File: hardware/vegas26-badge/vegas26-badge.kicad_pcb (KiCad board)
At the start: 2 copper layers, 100 x 145 mm, 41 parts, among them J1 FH34SRJ-24S-0.5SH(50)/(99) / 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, J2 AUDIO, J3 TC2050-IDC-NL / DNL, Q1 BSS138

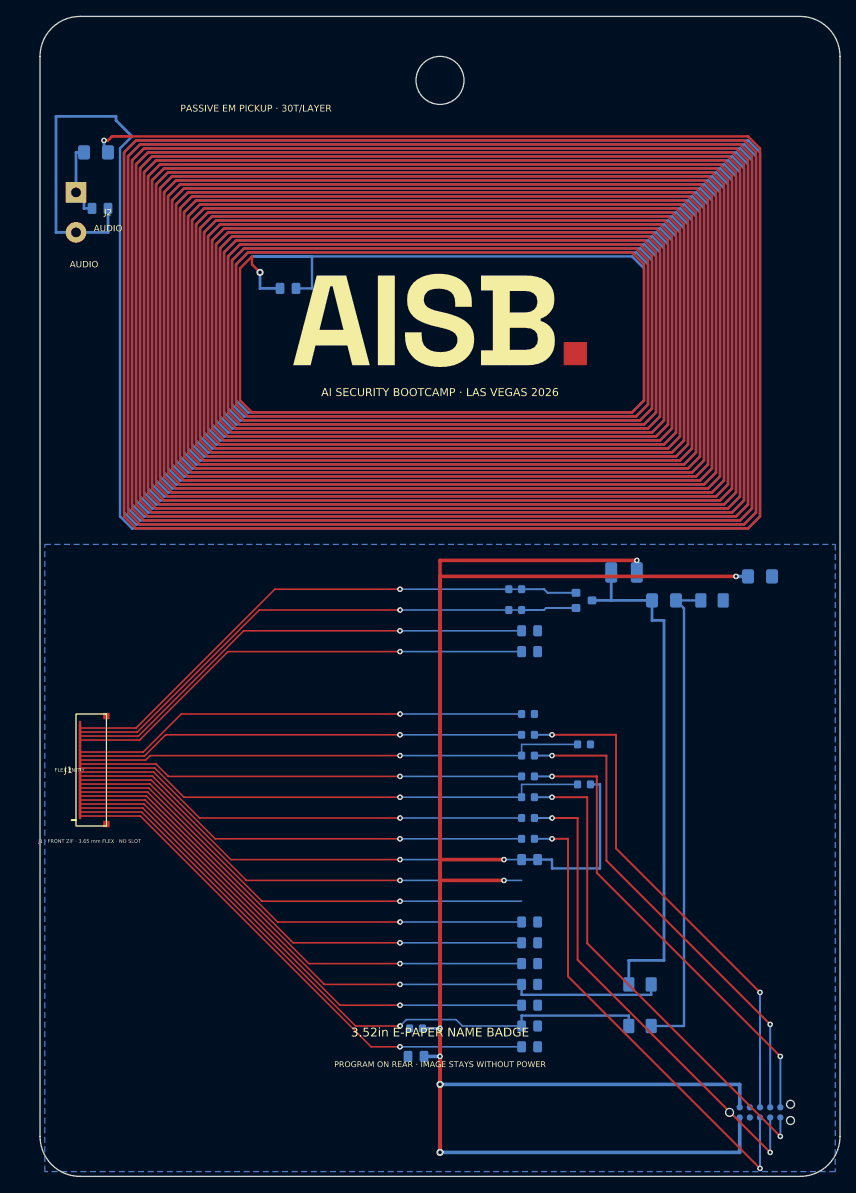
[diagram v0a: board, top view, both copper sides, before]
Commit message: Simplify ESP32 add-on to passive ribbon mount
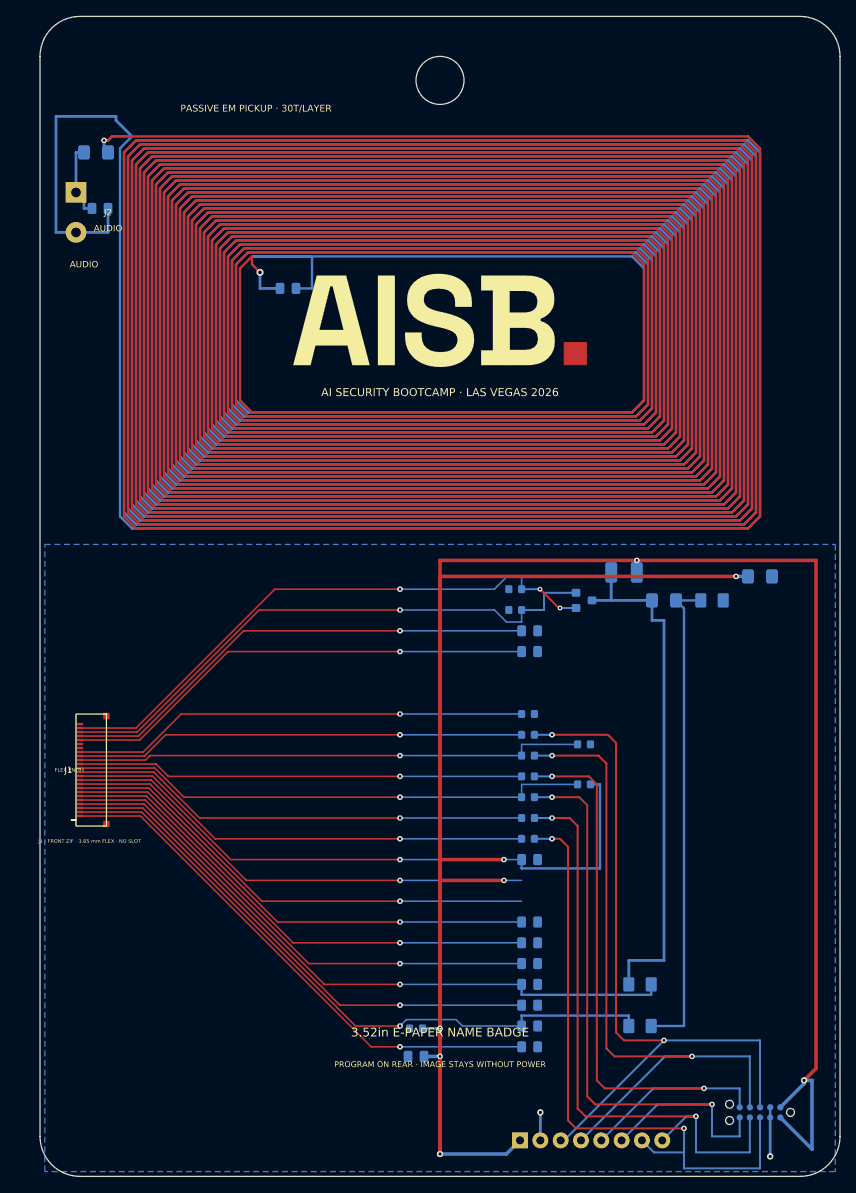
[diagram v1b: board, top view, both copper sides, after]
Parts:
- removed the MOD1 at (20.2, 120.9)
- removed the R3 at (59.4, 74.2)
- removed the R5 at (61.0, 102.8)
- removed the R6 at (61.0, 100.2)
- removed the R7 at (61.0, 97.6)
- added C13: 100nF, Badge:0603_C13, B.Cu at (47.0, 126.5)
- added C14: 1uF 10V, Badge:0805_C14, B.Cu at (61.2, 105.4)
- added C15: 1uF 25V / DNP, Badge:0805_C15, B.Cu at (61.2, 76.8)
- added D1: MBR0530, Badge:D_SOD-123, B.Cu at (84.0, 73.0)
- added J4: 1x08 P2.54 / OPTIONAL / DNP, Badge:ESP_Ribbon_1x08_P2.54mm, B.Cu at (60.0, 140.5)
- added L2: 68uH, Badge:1210_L2, B.Cu at (73.0, 69.5)
- added MH1: 4x 2.2x6 NPTH CRADLE SLOTS, Badge:ESP32_Cradle_Strap_Slots, B.Cu at (0.00, 0.00)
- C10: renamed from C15; value 1uF 25V / DNP -> 1uF 25V; footprint Badge:0805_C15 -> Badge:0805_C10
- C11: renamed from L2; value 68uH -> 1uF 25V; footprint Badge:1210_L2 -> Badge:0805_C11
- C12: renamed from D1; value MBR0530 -> 10uF 10V; footprint Badge:D_SOD-123 -> Badge:0805_C12
- C2: renamed from C7; value 1uF 25V -> 4.7uF 50V; footprint Badge:0805_C7 -> Badge:1206_C2
- C3: renamed from C8; value 1uF 25V -> 4.7uF 50V; footprint Badge:0805_C8 -> Badge:1206_C3
- C4: renamed from C9; footprint Badge:0805_C9 -> Badge:0805_C4
- C5: renamed from C10; value 1uF 25V -> 1uF 10V; footprint Badge:0805_C10 -> Badge:0805_C5
- C6: renamed from C11; footprint Badge:0805_C11 -> Badge:0805_C6
- C7: renamed from C12; value 10uF 10V -> 1uF 25V; footprint Badge:0805_C12 -> Badge:0805_C7
- C8: renamed from C13; value 100nF -> 1uF 25V; footprint Badge:0603_C13 -> Badge:0805_C8
- C9: renamed from C14; value 1uF 10V -> 1uF 25V; footprint Badge:0805_C14 -> Badge:0805_C9
- MOD1: renamed from R4; value 10k -> WAVESHARE E-PAPER ESP32 DRIVER BOARD V3 / OPTIONAL; footprint Badge:0603_R4 -> Badge:Waveshare_ESP32_Driver_Board_V3_Header_Clear_Cradle_Bay
- R10: renamed from C3; value 4.7uF 50V -> 1k; footprint Badge:1206_C3 -> Badge:0603_R10
- R11: renamed from C4; value 1uF 25V -> 100k; footprint Badge:0805_C4 -> Badge:0603_R11
- R12: renamed from C5; value 1uF 10V -> 100k; footprint Badge:0805_C5 -> Badge:0603_R12
- R13: renamed from C6; value 1uF 25V -> 0R; footprint Badge:0805_C6 -> Badge:0603_R13
- R3: renamed from R8; value 100R -> 3R; footprint Badge:0603_R8 -> Badge:0603_R3
- R4: renamed from R9; value 100R -> 10k; footprint Badge:0603_R9 -> Badge:0603_R4
- R5: renamed from R10; value 1k -> 100R; footprint Badge:0603_R10 -> Badge:0603_R5
- R6: renamed from R11; value 100k -> 100R; footprint Badge:0603_R11 -> Badge:0603_R6
- R7: renamed from R12; value 100k -> 100R; footprint Badge:0603_R12 -> Badge:0603_R7
- R8: renamed from R13; value 0R -> 100R; footprint Badge:0603_R13 -> Badge:0603_R8
- R9: renamed from C2; value 4.7uF 50V -> 100R; footprint Badge:1206_C2 -> Badge:0603_R9
- moved C12 68.0 mm to (47.0, 130.0)
- moved MOD1 62.9 mm to (20.2, 120.9)
- moved C11 60.5 mm to (61.2, 128.8)
- moved C2 56.3 mm to (90.0, 70.0)
- moved C3 50.9 mm to (78.0, 73.0)
- moved C10 49.4 mm to (61.2, 126.2)
- moved C4 44.2 mm to (61.2, 79.4)
- moved R9 36.6 mm to (61.0, 92.4)
- moved R13 28.6 mm to (61.0, 87.2)
- moved R10 23.9 mm to (61.0, 89.8)
- moved R12 23.2 mm to (68.0, 91.0)
- moved R4 20.9 mm to (59.4, 71.6)
- moved R3 20.9 mm to (59.4, 74.2)
- moved C7 18.3 mm to (61.2, 118.4)
- moved C9 18.2 mm to (61.2, 123.6)
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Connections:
- C10 pad 1: LEGACY_NC -> VGL
- C11 pad 1: SW -> VCOM
- C11 pad 2: 3V3 -> DGND
- C12 pad 2: CFLY -> 3V3
- C2 pad 1: VSH -> 3V3
- C3 pad 1: VGH -> SW
- C3 pad 2: DGND -> CFLY
- C4 pad 1: VSL -> VDHR
- C5 pad 1: VGL -> VDDD
- C6 pad 1: VCOM -> VPP
- C7 pad 1: DGND -> VSH
- C7 pad 2: 3V3 -> DGND
- C8 pad 1: DGND -> VGH
- C8 pad 2: 3V3 -> DGND
- C9 pad 1: 3V3 -> VSL
- R10 pad 1: SW -> EPD_BUSY
- R10 pad 2: CFLY -> EXT_BUSY
- R11 pad 1: VDHR -> EPD_CS
- R11 pad 2: DGND -> 3V3
- R12 pad 1: VDDD -> EPD_RST
- R13 pad 1: VPP -> BS
- R3 pad 1: EPD_DC -> DGND
- R3 pad 2: EXT_DC -> RESE
- R4 pad 1: EPD_RST -> DGND
- R4 pad 2: EXT_RST -> GDR
- R5 pad 1: EPD_BUSY -> EPD_MOSI
- R5 pad 2: EXT_BUSY -> EXT_MOSI
- R6 pad 1: EPD_CS -> EPD_CLK
- R6 pad 2: 3V3 -> EXT_CLK
- R7 pad 1: EPD_RST -> EPD_CS
- R7 pad 2: DGND -> EXT_CS
- R8 pad 1: BS -> EPD_DC
- R8 pad 2: DGND -> EXT_DC
- R9 pad 1: 3V3 -> EPD_RST
- R9 pad 2: DGND -> EXT_RST
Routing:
- net 3V3: track 382.9 -> 419.4 mm
- net EXT_BUSY: track 64.2 -> 91.7 mm
- net EXT_RST: track 61.4 -> 88.0 mm
- net EXT_DC: track 58.7 -> 81.4 mm
- net EXT_MOSI: track 61.7 -> 83.5 mm
- net EXT_CS: track 61.4 -> 82.4 mm
- net EXT_CLK: track 61.5 -> 77.4 mm
- net DGND: track 61.1 -> 70.7 mm, vias 1 -> 3
- net RESE: track 68.4 -> 72.6 mm
- net GDR: track 69.4 -> 72.3 mm, vias 1 -> 3
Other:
- board text added: "ONE CONTROLLER · 3V3 ONLY"
- board text added: "REV 2 · VERIFY PANEL/J1 + ESP CRADLE"
- board text removed: "ONE 3V3 SOURCE ONLY"
- board text removed: "REV 1 · PANEL/J1 FIT MUST BE VERIFIED"

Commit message: Save KiCad 10 badge board state
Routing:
- net 3V3: track 419.4 -> 407.2 mm
- net DGND: track 70.7 -> 80.1 mm, vias 3 -> 4

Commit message: Enlarge badge logo and add rear QR
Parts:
- moved ? 4.35 mm to (71.1, 43.2)
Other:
- board text added: "aisb.dev/badge0"
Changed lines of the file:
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@@
 		(at 50 38)
 		(property "Reference" "LOGO1"
-			(at 0 -7.2 0)
+			(at 0 -9 0)
 			(layer "F.Fab")
 			(effects
@@
 		)
 		(property "Value" "AISB OFFICIAL WORDMARK"
-			(at 0 7.2 0)
+			(at 0 9 0)
 			(layer "F.Fab")
 			(effects
@@
 		(fp_poly
 			(pts
-				(xy -7.764 5.6) (xy -7.764 -5.6) (xy -5.652 -5.6) (xy -5.652 5.6) (xy -7.764 5.6)
+				(xy -9.705 7) (xy -9.705 -7) (xy -7.065 -7) (xy -7.065 7) (xy -9.705 7)
 			)
 			(stroke
@@
 		(fp_poly
 			(pts
-				(xy -18.356 5.6) (xy -15.412 -5.6) (xy -11.732 -5.6) (xy -8.788 5.6) (xy -10.964 5.6) (xy -11.572 3.136)
-				(xy -15.076 3.136) (xy -15.076 1.184) (xy -12.068 1.184) (xy -13.428 -4.272) (xy -13.716 -4.272)
-				(xy -15.076 1.184) (xy -15.076 3.136) (xy -15.572 3.136) (xy -16.18 5.6) (xy -18.356 5.6)
+				(xy -22.945 7) (xy -19.265 -7) (xy -14.665 -7) (xy -10.985 7) (xy -13.705 7) (xy -14.465 3.92)
+				(xy -18.845 3.92) (xy -18.845 1.48) (xy -15.085 1.48) (xy -16.785 -5.34) (xy -17.145 -5.34)
+				(xy -18.845 1.48) (xy -18.845 3.92) (xy -19.465 3.92) (xy -20.225 7) (xy -22.945 7)
 			)
 			(stroke
@@
 		(fp_poly
 			(pts
-				(xy 5.132 5.6) (xy 5.132 3.744) (xy 6.604 3.744) (xy 6.604 -3.744) (xy 5.132 -3.744) (xy 5.132 -5.6)
-				(xy 10.892 -5.6) (xy 11.545 -5.562) (xy 12.14 -5.447) (xy 12.676 -5.256) (xy 13.145 -4.995) (xy 13.54 -4.669)
-				(xy 13.86 -4.28) (xy 14.096 -3.831) (xy 14.237 -3.327) (xy 14.284 -2.768) (xy 14.284 -2.608) (xy 14.252 -2.127)
-				(xy 14.156 -1.708) (xy 13.996 -1.352) (xy 13.682 -0.92) (xy 13.316 -0.6) (xy 12.934 -0.374) (xy 12.572 -0.224)
-				(xy 12.572 0.064) (xy 12.94 0.202) (xy 13.34 0.424) (xy 13.726 0.746) (xy 14.052 1.184) (xy 14.216 1.548)
-				(xy 14.315 1.98) (xy 14.348 2.48) (xy 14.348 2.64) (xy 14.3 3.229) (xy 14.156 3.76) (xy 13.916 4.232)
-				(xy 13.592 4.64) (xy 13.194 4.979) (xy 12.724 5.248) (xy 12.19 5.444) (xy 11.6 5.561) (xy 10.956 5.6)
-				(xy 8.716 5.6) (xy 8.716 -0.992) (xy 10.668 -0.992) (xy 11.266 -1.076) (xy 11.748 -1.328) (xy 12.066 -1.728)
-				(xy 12.172 -2.256) (xy 12.172 -2.416) (xy 12.068 -2.954) (xy 11.756 -3.352) (xy 11.276 -3.598) (xy 10.668 -3.68)
-				(xy 8.716 -3.68) (xy 8.716 -0.992) (xy 8.716 5.6) (xy 8.716 3.68) (xy 10.7 3.68) (xy 11.322 3.596)
-				(xy 11.812 3.344) (xy 12.13 2.936) (xy 12.236 2.384) (xy 12.236 2.224) (xy 12.132 1.672) (xy 11.82 1.264)
-				(xy 11.332 1.012) (xy 10.7 0.928) (xy 8.716 0.928) (xy 8.716 3.68) (xy 8.716 5.6) (xy 5.132 5.6)
+				(xy 6.415 7) (xy 6.415 4.68) (xy 8.255 4.68) (xy 8.255 -4.68) (xy 6.415 -4.68) (xy 6.415 -7)
+				(xy 13.615 -7) (xy 14.4313 -6.9525) (xy 15.175 -6.8087) (xy 15.845 -6.57) (xy 16.4312 -6.2438) (xy 16.925 -5.8362)
+				(xy 17.325 -5.35) (xy 17.62 -4.7888) (xy 17.7963 -4.1587) (xy 17.855 -3.46) (xy 17.855 -3.26) (xy 17.815 -2.6587)
+				(xy 17.695 -2.135) (xy 17.495 -1.69) (xy 17.1025 -1.15) (xy 16.645 -0.75) (xy 16.1675 -0.4675) (xy 15.715 -0.28)
+				(xy 15.715 0.08) (xy 16.175 0.2525) (xy 16.675 0.53) (xy 17.1575 0.9325) (xy 17.565 1.48) (xy 17.77 1.935)
+				(xy 17.8938 2.475) (xy 17.935 3.1) (xy 17.935 3.3) (xy 17.875 4.0362) (xy 17.695 4.7) (xy 17.395 5.29)
+				(xy 16.99 5.8) (xy 16.4925 6.2237) (xy 15.905 6.56) (xy 15.2375 6.805) (xy 14.5 6.9512) (xy 13.695 7)
+				(xy 10.895 7) (xy 10.895 -1.24) (xy 13.335 -1.24) (xy 14.0825 -1.345) (xy 14.685 -1.66) (xy 15.0825 -2.16)
+				(xy 15.215 -2.82) (xy 15.215 -3.02) (xy 15.085 -3.6925) (xy 14.695 -4.19) (xy 14.095 -4.4975) (xy 13.335 -4.6)
+				(xy 10.895 -4.6) (xy 10.895 -1.24) (xy 10.895 7) (xy 10.895 4.6) (xy 13.375 4.6) (xy 14.1525 4.495)
+				(xy 14.765 4.18) (xy 15.1625 3.67) (xy 15.295 2.98) (xy 15.295 2.78) (xy 15.165 2.09) (xy 14.775 1.58)
+				(xy 14.165 1.265) (xy 13.375 1.16) (xy 10.895 1.16) (xy 10.895 4.6) (xy 10.895 7) (xy 6.415 7)
 			)
 			(stroke
@@
 		(fp_poly
 			(pts
-				(xy 0.028 5.824) (xy -0.601 5.795) (xy -1.192 5.708) (xy -1.745 5.563) (xy -2.26 5.36) (xy -2.729 5.103)
-				(xy -3.144 4.796) (xy -3.505 4.439) (xy -3.812 4.032) (xy -4.057 3.578) (xy -4.232 3.08) (xy -4.337 2.538)
-				(xy -4.372 1.952) (xy -4.372 1.504) (xy -2.292 1.504) (xy -2.292 1.952) (xy -2.223 2.568) (xy -2.015 3.072)
-				(xy -1.668 3.464) (xy -1.202 3.744) (xy -0.637 3.912) (xy 0.028 3.968) (xy 0.692 3.92) (xy 1.233 3.776)
-				(xy 1.652 3.536) (xy 1.95 3.221) (xy 2.128 2.853) (xy 2.188 2.432) (xy 2.122 2.012) (xy 1.924 1.68)
-				(xy 1.6 1.418) (xy 1.156 1.208) (xy 0.796 1.088) (xy 0.388 0.973) (xy -0.068 0.864) (xy -0.436 0.784)
-				(xy -0.991 0.648) (xy -1.506 0.494) (xy -1.979 0.323) (xy -2.412 0.136) (xy -2.919 -0.153) (xy -3.34 -0.497)
-				(xy -3.676 -0.896) (xy -3.92 -1.365) (xy -4.067 -1.92) (xy -4.116 -2.56) (xy -4.062 -3.21) (xy -3.899 -3.794)
-				(xy -3.628 -4.312) (xy -3.258 -4.76) (xy -2.8 -5.133) (xy -2.252 -5.432) (xy -1.789 -5.604) (xy -1.286 -5.726)
-				(xy -0.744 -5.8) (xy -0.164 -5.824) (xy 0.42 -5.799) (xy 0.97 -5.722) (xy 1.488 -5.595) (xy 1.972 -5.416)
-				(xy 2.415 -5.187) (xy 2.808 -4.908) (xy 3.151 -4.579) (xy 3.444 -4.2) (xy 3.679 -3.771) (xy 3.846 -3.29)
-				(xy 3.947 -2.758) (xy 3.98 -2.176) (xy 3.98 -1.696) (xy 1.9 -1.696) (xy 1.9 -2.176) (xy 1.838 -2.754)
-				(xy 1.652 -3.208) (xy 1.35 -3.548) (xy 0.94 -3.784) (xy 0.432 -3.922) (xy -0.164 -3.968) (xy -0.748 -3.928)
-				(xy -1.22 -3.808) (xy -1.58 -3.608) (xy -1.922 -3.182) (xy -2.036 -2.624) (xy -1.982 -2.24) (xy -1.82 -1.92)
-				(xy -1.55 -1.656) (xy -1.172 -1.44) (xy -0.68 -1.26) (xy -0.068 -1.104) (xy 0.3 -1.024) (xy 0.881 -0.887)
-				(xy 1.422 -0.732) (xy 1.924 -0.559) (xy 2.388 -0.368) (xy 2.936 -0.073) (xy 3.398 0.279) (xy 3.772 0.688)
-				(xy 4.048 1.166) (xy 4.213 1.726) (xy 4.268 2.368) (xy 4.236 2.865) (xy 4.138 3.33) (xy 3.976 3.765)
-				(xy 3.748 4.168) (xy 3.461 4.535) (xy 3.12 4.86) (xy 2.725 5.143) (xy 2.276 5.384) (xy 1.779 5.577)
-				(xy 1.238 5.714) (xy 0.654 5.797) (xy 0.028 5.824)
+				(xy 0.035 7.28) (xy -0.7512 7.2438) (xy -1.49 7.135) (xy -2.1813 6.9537) (xy -2.825 6.7) (xy -3.4112 6.3788)
+				(xy -3.93 5.995) (xy -4.3812 5.5488) (xy -4.765 5.04) (xy -5.0713 4.4725) (xy -5.29 3.85) (xy -5.4212 3.1725)
+				(xy -5.465 2.44) (xy -5.465 1.88) (xy -2.865 1.88) (xy -2.865 2.44) (xy -2.7787 3.21) (xy -2.5188 3.84)
+				(xy -2.085 4.33) (xy -1.5025 4.68) (xy -0.7963 4.89) (xy 0.035 4.96) (xy 0.865 4.9) (xy 1.5413 4.72)
+				(xy 2.065 4.42) (xy 2.4375 4.0263) (xy 2.66 3.5663) (xy 2.735 3.04) (xy 2.6525 2.515) (xy 2.405 2.1)
+				(xy 2 1.7725) (xy 1.445 1.51) (xy 0.995 1.36) (xy 0.485 1.2163) (xy -0.085 1.08) (xy -0.545 0.98)
+				(xy -1.2388 0.81) (xy -1.8825 0.6175) (xy -2.4737 0.4037) (xy -3.015 0.17) (xy -3.6488 -0.1913) (xy -4.175 -0.6212)
+				(xy -4.595 -1.12) (xy -4.9 -1.7063) (xy -5.0838 -2.4) (xy -5.145 -3.2) (xy -5.0775 -4.0125) (xy -4.8738 -4.7425)
+				(xy -4.535 -5.39) (xy -4.0725 -5.95) (xy -3.5 -6.4162) (xy -2.815 -6.79) (xy -2.2363 -7.005) (xy -1.6075 -7.1575)
+				(xy -0.93 -7.25) (xy -0.205 -7.28) (xy 0.525 -7.2488) (xy 1.2125 -7.1525) (xy 1.86 -6.9937) (xy 2.465 -6.77)
+				(xy 3.0187 -6.4838) (xy 3.51 -6.135) (xy 3.9387 -5.7237) (xy 4.305 -5.25) (xy 4.5987 -4.7138) (xy 4.8075 -4.1125)
+				(xy 4.9337 -3.4475) (xy 4.975 -2.72) (xy 4.975 -2.12) (xy 2.375 -2.12) (xy 2.375 -2.72) (xy 2.2975 -3.4425)
+				(xy 2.065 -4.01) (xy 1.6875 -4.435) (xy 1.175 -4.73) (xy 0.54 -4.9025) (xy -0.205 -4.96) (xy -0.935 -4.91)
+				(xy -1.525 -4.76) (xy -1.975 -4.51) (xy -2.4025 -3.9775) (xy -2.545 -3.28) (xy -2.4775 -2.8) (xy -2.275 -2.4)
+				(xy -1.9375 -2.07) (xy -1.465 -1.8) (xy -0.85 -1.575) (xy -0.085 -1.38) (xy 0.375 -1.28) (xy 1.1013 -1.1088)
+				(xy 1.7775 -0.915) (xy 2.405 -0.6988) (xy 2.985 -0.46) (xy 3.67 -0.0912) (xy 4.2475 0.3488) (xy 4.715 0.86)
+				(xy 5.06 1.4575) (xy 5.2663 2.1575) (xy 5.335 2.96) (xy 5.295 3.5813) (xy 5.1725 4.1625) (xy 4.97 4.7062)
+				(xy 4.685 5.21) (xy 4.3262 5.6688) (xy 3.9 6.075) (xy 3.4063 6.4287) (xy 2.845 6.73) (xy 2.2237 6.9712)
+				(xy 1.5475 7.1425) (xy 0.8175 7.2462) (xy 0.035 7.28)
 			)
 			(stroke
@@
 	(footprint "Badge:Gold_Brand_Accent"
 		(layer "F.Cu")
-		(at 66.906 42.15)
+		(at 71.1325 43.1875)
 		(property "Reference" ""
 			(at 0 0 0)
@@
 		(pad "" smd roundrect
 			(at 0 0)
-			(size 2.9 2.9)
+			(size 3.625 3.625)
 			(layers "F.Cu" "F.Mask")
 			(roundrect_rratio 0.02)
@@
 		)
 	)
+	(barcode
+		(at 21 79.2 0)
+		(layer "B.SilkS")
+		(size 20 20)
+		(text "https://aisb.dev/badge0")
+		(text_height 1)
+		(type qr)
+		(ecc_level M)
+		(hide yes)
+		(knockout yes)
+		(margins 3.2 3.2)
+	)
+	(gr_text "aisb.dev/badge0"
+		(at 21 94.5 0)
+		(layer "B.SilkS")
+		(effects
+			(font
+				(size 1 1)
+				(thickness 0.15)
+			)
+			(justify mirror)
+		)
+	)

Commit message: Track current badge design and assembly snapshot
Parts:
- removed LOGO1: AISB OFFICIAL WORDMARK, Badge:AISB_Logo_Vector
- moved L1 16.4 mm to (40.1, 26.0)
- moved C11 5.00 mm to (61.2, 123.8)
- moved C10 5.00 mm to (61.2, 121.2)
- moved C12 5.00 mm to (47.0, 125.0)
- moved C13 5.00 mm to (47.0, 121.5)
- moved C14 5.00 mm to (61.2, 100.4)
- moved C5 5.00 mm to (61.2, 108.2)
- moved C6 5.00 mm to (61.2, 110.8)
- moved C7 5.00 mm to (61.2, 113.4)
- moved C8 5.00 mm to (61.2, 116.0)
- moved C9 5.00 mm to (61.2, 118.6)
- moved D2 5.00 mm to (75.0, 121.2)
- moved D3 5.00 mm to (75.0, 116.0)
- moved EPD1 5.00 mm to (50.0, 89.2)
- moved J3 5.00 mm to (90.0, 132.0)
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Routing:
- net 3V3: track 407.2 -> 322.9 mm, vias 10 -> 8
- net DGND: track 80.1 -> 62.8 mm
- net CFLY: track 60.8 -> 55.4 mm
- net SW: track 64.9 -> 59.9 mm
- net VSH: track 63.7 -> 61.6 mm
- net EPD_RST: track 63.8 -> 65.9 mm
- net VSL: track 65.4 -> 63.3 mm
- net VPP: track 62.8 -> 60.7 mm
- net VGH: track 83.3 -> 81.3 mm
- net VDDD: track 61.9 -> 59.9 mm
- net VCOM: track 67.1 -> 65.1 mm
- net EPD_MOSI: track 58.4 -> 56.4 mm
- net EPD_CLK: track 57.6 -> 55.5 mm
- net EPD_BUSY: track 56.3 -> 58.4 mm
- net BS: track 57.2 -> 59.2 mm
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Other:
- board text added: "aisb.dev"
- board text removed: "3.52in E-PAPER NAME BADGE"
- board text removed: "J1 · FRONT ZIF · 3.65 mm FLEX · NO SLOT"
- board text removed: "J3 · TC2050"
- board text removed: "PROGRAM ON REAR · IMAGE STAYS WITHOUT POWER"
- board text removed: "REV 2 · VERIFY PANEL/J1 + ESP CRADLE"
- board text removed: "aisb.dev/badge0"

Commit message: new badge
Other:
- board text added: "3V3"
- board text added: "AI SECURITY BOOTCAMP · LONDON 2026"
- board text added: "DGND"
- board text added: "EXT_BUSY"
- board text added: "EXT_CLK"
- board text added: "EXT_CS"
- board text added: "EXT_DC"
- board text added: "EXT_MOSI"
- board text added: "EXT_RST"
- board text removed: "AI SECURITY BOOTCAMP · LAS VEGAS 2026"
- board text removed: "AUDIO"
- board text removed: "ONE CONTROLLER · 3V3 ONLY"
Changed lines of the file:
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@@
 			(drillshape 0)
 			(scaleselection 1)
-			(outputdirectory "out")
+			(outputdirectory "out-london")
 		)
 	)
@@
 		(at 4.5 22)
 		(property "Reference" "J2"
-			(at 4 2.5 0)
+			(at 0 -4 0)
 			(layer "F.SilkS")
 			(effects
@@
 		)
 		(property "Value" "AUDIO"
-			(at 4 4.5 0)
+			(at 0 -2.5 0)
 			(layer "F.SilkS")
 			(effects
@@
 		)
 		(property "Value" "1x08 P2.54 / OPTIONAL / DNP"
-			(at 8.89 2.2 0)
+			(at 0 4 0)
 			(layer "B.Fab")
 			(effects
@@
 		)
 		(fp_text user "ESP RIBBON · 3V3 ONLY"
-			(at 8.89 -2.2 0)
+			(at 0 -2.5 0)
 			(layer "B.SilkS")
 			(effects
@@
 		(layer "Edge.Cuts")
 	)
-	(gr_text "AUDIO"
-		(at 5.5 31 0)
-		(layer "F.SilkS")
-		(effects
-			(font
-				(size 0.8 0.8)
-				(thickness 0.15)
-			)
-		)
-	)
 	(gr_text "PASSIVE EM PICKUP · 30T/LAYER"
 		(at 26 14 0)
@@
 		)
 	)
-	(gr_text "AI SECURITY BOOTCAMP · LAS VEGAS 2026"
+	(gr_text "AI SECURITY BOOTCAMP · LONDON 2026"
 		(at 49 48 0)
 		(layer "F.SilkS")
@@
 		)
 	)
-	(gr_text "ONE CONTROLLER · 3V3 ONLY"
-		(at 68 134.5 0)
+	(gr_text "3V3"
+		(at 60 138 270)
 		(layer "B.SilkS")
 		(effects
 			(font
-				(size 0.62 0.62)
-				(thickness 0.13)
+				(size 0.65 0.65)
+				(thickness 0.15)
+			)
+			(justify mirror)
+		)
+	)
+	(gr_text "DGND"
+		(at 62.571429 138.417857 270)
+		(layer "B.SilkS")
+		(effects
+			(font
+				(size 0.65 0.65)
+				(thickness 0.15)
+			)
+			(justify mirror)
+		)
+	)
+	(gr_text "EXT_BUSY"
+		(at 65.142857 139.454762 270)
+		(layer "B.SilkS")
+		(effects
+			(font
+				(size 0.65 0.65)
+				(thickness 0.15)
+			)
+			(justify mirror)
+		)
+	)
+	(gr_text "EXT_RST"
+		(at 67.714286 139.083333 270)
+		(layer "B.SilkS")
+		(effects
+			(font
+				(size 0.65 0.65)
+				(thickness 0.15)
+			)
+			(justify mirror)
+		)
+	)
+	(gr_text "EXT_DC"
+		(at 70.285714 138.85119 270)
+		(layer "B.SilkS")
+		(effects
+			(font
+				(size 0.65 0.65)
+				(thickness 0.15)
+			)
+			(justify mirror)
+		)
+	)
+	(gr_text "EXT_CS"
+		(at 72.857143 138.835714 270)
+		(layer "B.SilkS")
+		(effects
+			(font
+				(size 0.65 0.65)
+				(thickness 0.15)
+			)
+			(justify mirror)
+		)
+	)
+	(gr_text "EXT_MOSI"
+		(at 75.428571 139.377381 270)
+		(layer "B.SilkS")
+		(effects
+			(font
+				(size 0.65 0.65)
+				(thickness 0.15)
+			)
+			(justify mirror)
+		)
+	)
+	(gr_text "EXT_CLK"
+		(at 78 139.114285 270)
+		(layer "B.SilkS")
+		(effects
+			(font
+				(size 0.65 0.65)
+				(thickness 0.15)
 			)
 			(justify mirror)
